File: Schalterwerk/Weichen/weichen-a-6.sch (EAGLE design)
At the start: 46 parts, among them Q1 P-MOSFET, Q2 P-MOSFET, X1 PHNX_4P_508CONN_1017493, X2 IO-HAT, X3 PHNX_4P_350CONN_1984989_PXC, X4 PHNX_4P_350CONN_1984989_PXC, X5 RJ45-JACK

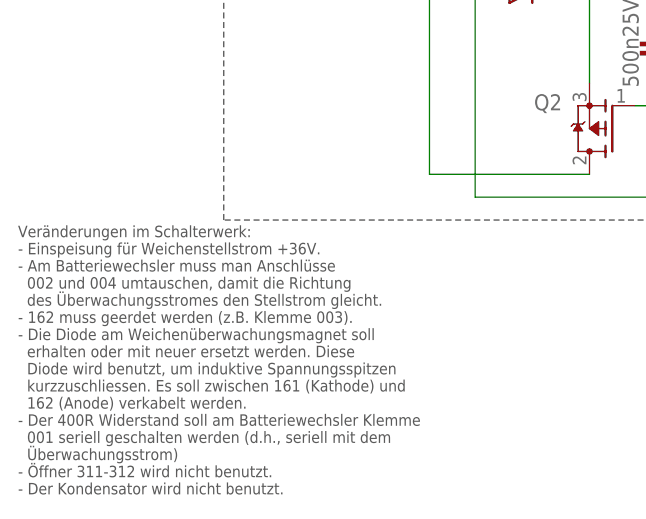
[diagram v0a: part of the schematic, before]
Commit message: Fixes instructions on the weichen rework.
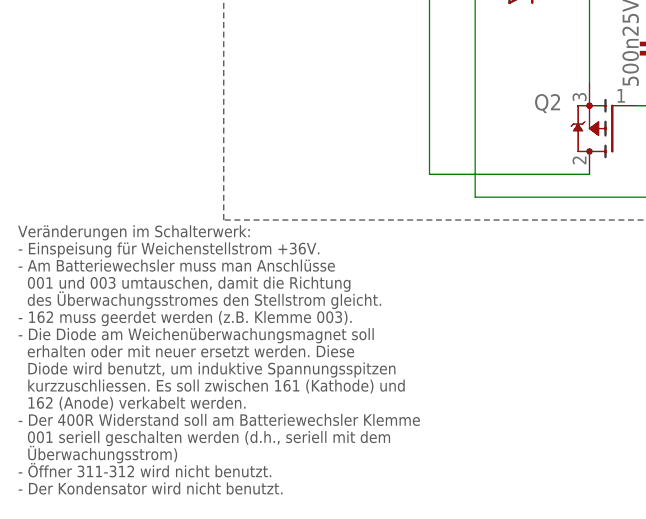
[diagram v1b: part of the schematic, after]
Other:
- note added: "Veränderungen im Schalterwerk: - Einspeisung für Weichenstellstrom +36V. - Am Batteriewechsler muss man Anschlüsse 001 und 003 umtauschen, damit die Richtung des Überwachungsstromes den Stellstrom gleicht. - 162 muss geerdet werden (z.B. Klemme 003). - Die Diode am Weichenüberwachungsmagnet soll erhalten oder mit neuer ersetzt werden. Diese Diode wird benutzt, um induktive Spannungsspitzen kurzzu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"
- note removed: "Veränderungen im Schalterwerk: - Einspeisung für Weichenstellstrom +36V. - Am Batteriewechsler muss man Anschlüsse 002 und 004 umtauschen, damit die Richtung des Überwachungsstromes den Stellstrom gleicht. - 162 muss geerdet werden (z.B. Klemme 003). - Die Diode am Weichenüberwachungsmagnet soll erhalten oder mit neuer ersetzt werden. Diese Diode wird benutzt, um induktive Spannungsspitzen kurzzu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"
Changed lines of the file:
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@@
 - Einspeisung für Weichenstellstrom +36V.
 - Am Batteriewechsler muss man Anschlüsse
-  002 und 004 umtauschen, damit die Richtung
+  001 und 003 umtauschen, damit die Richtung
   des Überwachungsstromes den Stellstrom gleicht.
 - 162 muss geerdet werden (z.B. Klemme 003).
